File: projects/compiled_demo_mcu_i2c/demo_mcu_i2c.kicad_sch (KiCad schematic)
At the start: 10 parts, among them U1 ATmega328, Y1 16MHz

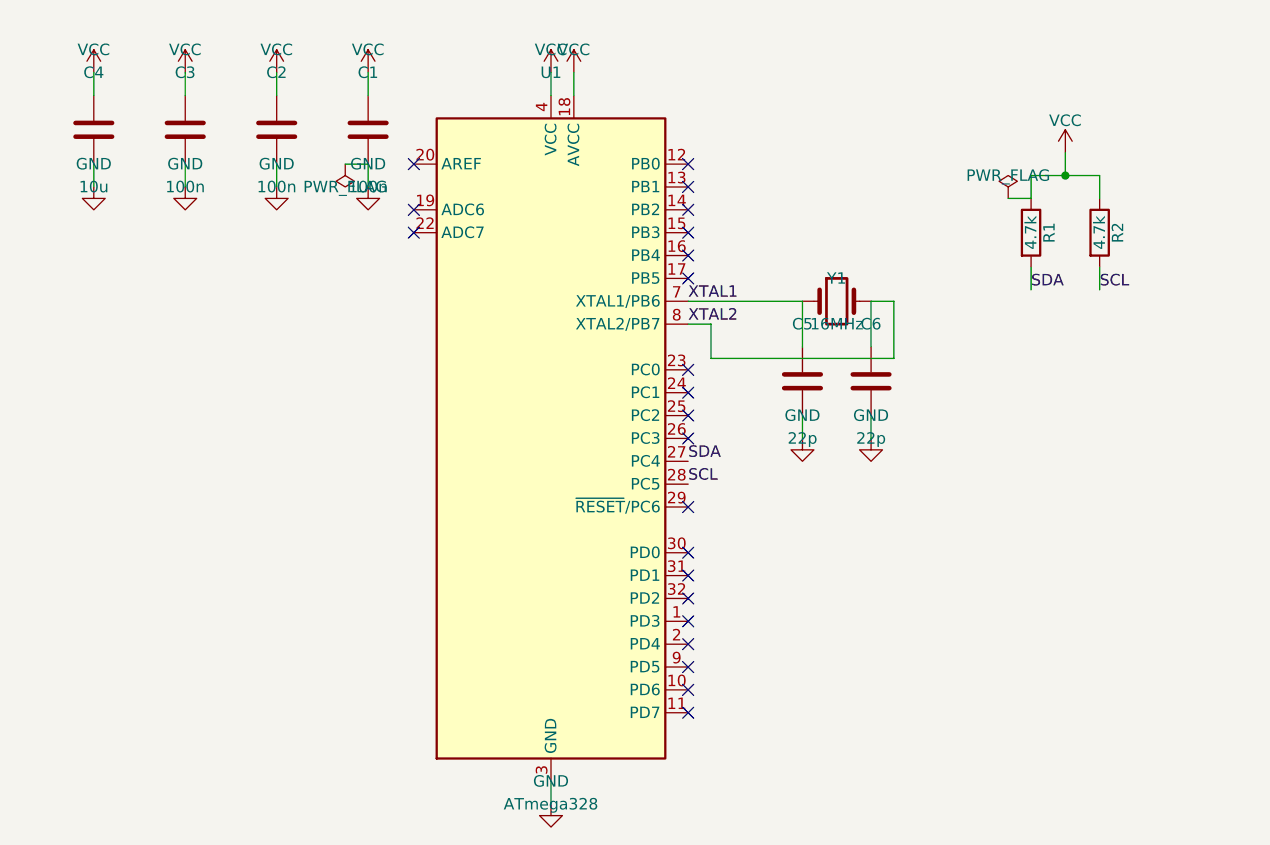
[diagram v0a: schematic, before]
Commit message: F3d+F3e: multi-unit parts and the textplace field autoplacer
Multi-unit: one Symbol per unit (shared ref+lib, distinct unit); nets and
anchors qualify pins as "REF.unit.pin". Resolver targets a specific placed
unit; the geometry probe instantiates per unit. NE5532 (units A/B/C)
compiles first try with both feedback loops wired.

textplace (internal/place2/textplace): deterministic text autoplacement run
at the end of compilation — every visible Reference/Value block is re-placed
horizontally at the least-overlapping side of its body, colliding net labels
flip around their anchor. Fixes the text-collision family the user flagged
on the buck render. KiCad gotcha baked into the pass: a field's drawn angle
is field+symbol rotation, so fields on 90/270 symbols carry a compensating
90 to display horizontal.

All 7 reference circuits now compile from declarative sources with clean
text. Gate demotions (buck SW, ne555 THR/DISCH) are by-design label
fallbacks, zero geometry violations everywhere.

Co-Authored-By: Claude Fable 5 <noreply@anthropic.com>
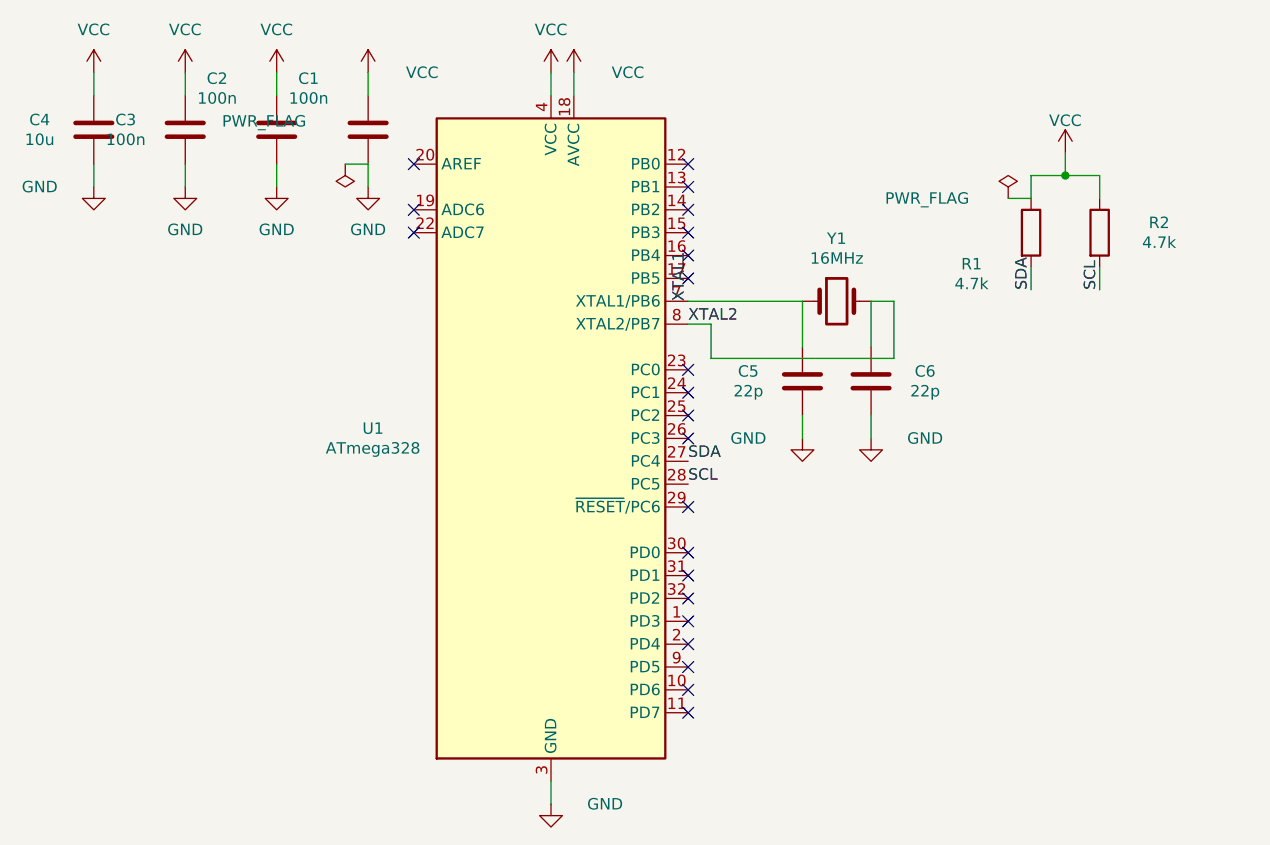
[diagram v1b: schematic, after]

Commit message: Body model sees real symbol graphics; quiet nets drop junction tags
User-reported flaws from visual review, both fixed at the root:

- Wires over symbol artwork: the body model was pin-derived and blind to
  drawn graphics — an op-amp triangle's vertices stick out beyond the pin
  box, so "legal" wires crossed the drawing. internal/sexp/graphics.go now
  parses rectangle/polyline/circle/arc/bezier extents per unit with the
  exact pin transform; metrics.BodyBBox unions them with the legacy box,
  clamped off pin tips (Device:LED's emission arrows overhang the cathode
  pin and would have swallowed it). NE5532 feedback: 8 stroke crossings
  through the triangle before, 0 after (loops now label pairs). The model
  also exposed genuinely bad baked geometry in mcu_minimal_atmega328's
  crystal — repositioned with the template contract intact.

- "ANODE" tag on a resistor leg: net names with a "_" prefix are now
  quiet — connectivity only, their documentation label is stripped at the
  end of compilation when the wiring alone keeps the net whole. Junction
  nodes (R->LED) stay unlabeled like in any hand-drawn schematic.

- Battery hump: led_18650 anchors R1 in the pin's exit direction; the
  design guide gains the "respect the pin's exit direction" and "internal
  junctions carry no tag" recipes.

Co-Authored-By: Claude Fable 5 <noreply@anthropic.com>
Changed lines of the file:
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@@
     (instances
       (project ""
-        (path "/49380d2c-6cd5-4ba7-9acf-a85711615e41" (reference "U1") (unit 1)))))
+        (path "/934af4ad-ced9-4f64-bf1b-10878731275e" (reference "U1") (unit 1)))))
   (symbol (lib_id "Device:C")
     (at 58.42 29.21 0) (unit 1) (exclude_from_sim no) (in_bom yes) (on_board yes) (dnp no)
@@
     (instances
       (project ""
-        (path "/49380d2c-6cd5-4ba7-9acf-a85711615e41" (reference "C1") (unit 1)))))
+        (path "/934af4ad-ced9-4f64-bf1b-10878731275e" (reference "C1") (unit 1)))))
   (symbol (lib_id "Device:C")
     (at 48.26 29.21 0) (unit 1) (exclude_from_sim no) (in_bom yes) (on_board yes) (dnp no)
@@
     (instances
       (project ""
-        (path "/49380d2c-6cd5-4ba7-9acf-a85711615e41" (reference "C2") (unit 1)))))
+        (path "/934af4ad-ced9-4f64-bf1b-10878731275e" (reference "C2") (unit 1)))))
   (symbol (lib_id "Device:C")
     (at 38.1 29.21 0) (unit 1) (exclude_from_sim no) (in_bom yes) (on_board yes) (dnp no)
@@
     (instances
       (project ""
-        (path "/49380d2c-6cd5-4ba7-9acf-a85711615e41" (reference "C3") (unit 1)))))
+        (path "/934af4ad-ced9-4f64-bf1b-10878731275e" (reference "C3") (unit 1)))))
   (symbol (lib_id "Device:C")
     (at 27.94 29.21 0) (unit 1) (exclude_from_sim no) (in_bom yes) (on_board yes) (dnp no)
@@
     (instances
       (project ""
-        (path "/49380d2c-6cd5-4ba7-9acf-a85711615e41" (reference "C4") (unit 1)))))
+        (path "/934af4ad-ced9-4f64-bf1b-10878731275e" (reference "C4") (unit 1)))))
   (symbol (lib_id "Device:Crystal")
     (at 109.22 52.07 270) (unit 1) (exclude_from_sim no) (in_bom yes) (on_board yes) (dnp no)
@@
     (instances
       (project ""
-        (path "/49380d2c-6cd5-4ba7-9acf-a85711615e41" (reference "Y1") (unit 1)))))
+        (path "/934af4ad-ced9-4f64-bf1b-10878731275e" (reference "Y1") (unit 1)))))
   (symbol (lib_id "Device:C")
     (at 120.65 48.26 90) (unit 1) (exclude_from_sim no) (in_bom yes) (on_board yes) (dnp no)
@@
     (instances
       (project ""
-        (path "/49380d2c-6cd5-4ba7-9acf-a85711615e41" (reference "C5") (unit 1)))))
+        (path "/934af4ad-ced9-4f64-bf1b-10878731275e" (reference "C5") (unit 1)))))
   (symbol (lib_id "Device:C")
     (at 120.65 55.88 90) (unit 1) (exclude_from_sim no) (in_bom yes) (on_board yes) (dnp no)
@@
     (instances
       (project ""
-        (path "/49380d2c-6cd5-4ba7-9acf-a85711615e41" (reference "C6") (unit 1)))))
+        (path "/934af4ad-ced9-4f64-bf1b-10878731275e" (reference "C6") (unit 1)))))
   (symbol (lib_id "Device:R")
     (at 139.7 40.64 0) (unit 1) (exclude_from_sim no) (in_bom yes) (on_board yes) (dnp no)
     (property "Reference" "R1"
-      (at 133.09 44.13 0)
+      (at 133.09 39.54 0)
       (effects
         (font (size 1.27 1.27))))
     (property "Value" "4.7k"
-      (at 133.09 46.33 0)
+      (at 133.09 41.74 0)
       (effects
         (font (size 1.27 1.27))))
@@
     (instances
       (project ""
-        (path "/49380d2c-6cd5-4ba7-9acf-a85711615e41" (reference "R1") (unit 1)))))
+        (path "/934af4ad-ced9-4f64-bf1b-10878731275e" (reference "R1") (unit 1)))))
   (symbol (lib_id "Device:R")
     (at 147.32 40.64 0) (unit 1) (exclude_from_sim no) (in_bom yes) (on_board yes) (dnp no)
@@
     (instances
       (project ""
-        (path "/49380d2c-6cd5-4ba7-9acf-a85711615e41" (reference "R2") (unit 1)))))
+        (path "/934af4ad-ced9-4f64-bf1b-10878731275e" (reference "R2") (unit 1)))))
   (symbol (lib_id "power:VCC")
     (at 143.51 31.75 0) (unit 1) (exclude_from_sim no) (in_bom no) (on_board no) (dnp no)
@@
     (instances
       (project ""
-        (path "/49380d2c-6cd5-4ba7-9acf-a85711615e41" (reference "#PWR1") (unit 1)))))
+        (path "/934af4ad-ced9-4f64-bf1b-10878731275e" (reference "#PWR1") (unit 1)))))
   (wire
     (pts (xy 139.7 34.29) (xy 143.51 34.29))
@@
     (instances
       (project ""
-        (path "/49380d2c-6cd5-4ba7-9acf-a85711615e41" (reference "#PWR02") (unit 1)))))
+        (path "/934af4ad-ced9-4f64-bf1b-10878731275e" (reference "#PWR02") (unit 1)))))
   (wire
     (pts (xy 78.74 101.6) (xy 78.74 104.14))
@@
     (instances
       (project ""
-        (path "/49380d2c-6cd5-4ba7-9acf-a85711615e41" (reference "#PWR03") (unit 1)))))
+        (path "/934af4ad-ced9-4f64-bf1b-10878731275e" (reference "#PWR03") (unit 1)))))
   (wire
     (pts (xy 58.42 33.02) (xy 58.42 35.56))
@@
     (instances
       (project ""
-        (path "/49380d2c-6cd5-4ba7-9acf-a85711615e41" (reference "#PWR04") (unit 1)))))
+        (path "/934af4ad-ced9-4f64-bf1b-10878731275e" (reference "#PWR04") (unit 1)))))
   (wire
     (pts (xy 48.26 33.02) (xy 48.26 35.56))
@@
     (instances
       (project ""
-        (path "/49380d2c-6cd5-4ba7-9acf-a85711615e41" (reference "#PWR05") (unit 1)))))
+        (path "/934af4ad-ced9-4f64-bf1b-10878731275e" (reference "#PWR05") (unit 1)))))
   (wire
     (pts (xy 38.1 33.02) (xy 38.1 35.56))
@@
     (instances
       (project ""
-        (path "/49380d2c-6cd5-4ba7-9acf-a85711615e41" (reference "#PWR06") (unit 1)))))
+        (path "/934af4ad-ced9-4f64-bf1b-10878731275e" (reference "#PWR06") (unit 1)))))
   (wire
     (pts (xy 27.94 33.02) (xy 27.94 35.56))
@@
     (instances
       (project ""
-        (path "/49380d2c-6cd5-4ba7-9acf-a85711615e41" (reference "#PWR07") (unit 1)))))
+        (path "/934af4ad-ced9-4f64-bf1b-10878731275e" (reference "#PWR07") (unit 1)))))
   (wire
     (pts (xy 124.46 48.26) (xy 127 48.26))
@@
     (instances
       (project ""
-        (path "/49380d2c-6cd5-4ba7-9acf-a85711615e41" (reference "#PWR08") (unit 1)))))
+        (path "/934af4ad-ced9-4f64-bf1b-10878731275e" (reference "#PWR08") (unit 1)))))
   (wire
     (pts (xy 124.46 55.88) (xy 127 55.88))
@@
     (instances
       (project ""
-        (path "/49380d2c-6cd5-4ba7-9acf-a85711615e41" (reference "#PWR09") (unit 1)))))
+        (path "/934af4ad-ced9-4f64-bf1b-10878731275e" (reference "#PWR09") (unit 1)))))
   (wire
     (pts (xy 78.74 25.4) (xy 78.74 22.86))
@@
     (instances
       (project ""
-        (path "/49380d2c-6cd5-4ba7-9acf-a85711615e41" (reference "#PWR10") (unit 1)))))
+        (path "/934af4ad-ced9-4f64-bf1b-10878731275e" (reference "#PWR10") (unit 1)))))
   (wire
     (pts (xy 81.28 25.4) (xy 81.28 22.86))
@@
     (instances
       (project ""
-        (path "/49380d2c-6cd5-4ba7-9acf-a85711615e41" (reference "#PWR11") (unit 1)))))
+        (path "/934af4ad-ced9-4f64-bf1b-10878731275e" (reference "#PWR11") (unit 1)))))
   (wire
     (pts (xy 58.42 25.4) (xy 58.42 22.86))
@@
     (instances
       (project ""
-        (path "/49380d2c-6cd5-4ba7-9acf-a85711615e41" (reference "#PWR12") (unit 1)))))
+        (path "/934af4ad-ced9-4f64-bf1b-10878731275e" (reference "#PWR12") (unit 1)))))
   (wire
     (pts (xy 48.26 25.4) (xy 48.26 22.86))
@@
     (instances
       (project ""
-        (path "/49380d2c-6cd5-4ba7-9acf-a85711615e41" (reference "#PWR13") (unit 1)))))
+        (path "/934af4ad-ced9-4f64-bf1b-10878731275e" (reference "#PWR13") (unit 1)))))
   (wire
     (pts (xy 38.1 25.4) (xy 38.1 22.86))
@@
     (instances
       (project ""
-        (path "/49380d2c-6cd5-4ba7-9acf-a85711615e41" (reference "#PWR14") (unit 1)))))
+        (path "/934af4ad-ced9-4f64-bf1b-10878731275e" (reference "#PWR14") (unit 1)))))
   (wire
     (pts (xy 27.94 25.4) (xy 27.94 22.86))
@@
     (instances
       (project ""
-        (path "/49380d2c-6cd5-4ba7-9acf-a85711615e41" (reference "#FLG01") (unit 1)))))
+        (path "/934af4ad-ced9-4f64-bf1b-10878731275e" (reference "#FLG01") (unit 1)))))
   (wire
     (pts (xy 58.42 33.02) (xy 55.88 33.02))
@@
     (instances
       (project ""
-        (path "/49380d2c-6cd5-4ba7-9acf-a85711615e41" (reference "#FLG02") (unit 1)))))
+        (path "/934af4ad-ced9-4f64-bf1b-10878731275e" (reference "#FLG02") (unit 1)))))
   (wire
     (pts (xy 139.7 36.83) (xy 137.16 36.83))
